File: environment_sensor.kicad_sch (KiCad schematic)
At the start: 121 parts, among them J1001 USB-C_USB4105-GF-A, J1002 SM04B-SRSS-TB-LF-SN, J1003 SM04B-SRSS-TB-LF-SN, U1001 FT4232H_VQFN, U1002 AP7370-33SA-7, U1003 STM32G474CET6, U1004 MB85RC1MTPNF-G, U1005 SHT45, U1006 BME280, Y1001 ABM3B-12.000MHZ-B2-T, Y1002 ECS-_327-12_5-34B-TR, Y1003 ABM3B-8.000MHZ-10-1-U-T

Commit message: Renumerate env sensor
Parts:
- renumbered BAT1001 to BAT1, C1038 to C104, C1039 to C105, C1040 to C106, C1001 to C56, C1002 to C57, C1003 to C59, C1004 to C60, C1005 to C62, C1006 to C63, C1007 to C64, C1008 to C65, C1009 to C67, C1010 to C68, C1011 to C69, C1012 to C70, C1013 to C71, C1014 to C72, C1015 to C73, C1016 to C74, C1017 to C75, C1018 to C76, C1019 to C77, C1020 to C78, C1021 to C79, C1022 to C80, C1023 to C81, C1024 to C82, C1025 to C83, C1026 to C84, C1027 to C85, C1028 to C86, C1029 to C87, C1030 to C88, C1031 to C89, C1032 to C90, C1033 to C91, C1034 to C92, C1035 to C93, C1036 to C94, C1037 to C95, D1001 to D36, D1002 to D37, D1003 to D38, D1004 to D39, D1005 to D40, D1006 to D41, D1007 to D42, D1008 to D43, D1009 to D44, FB1001 to FB13, FB1002 to FB14, FB1003 to FB15, FB1004 to FB16, FB1005 to FB17, J1001 to J17, J1002 to J18, J1003 to J20, LD1001 to LD1, LD1002 to LD2, MP1001 to MP10, MP1002 to MP11, MP1003 to MP12, R1001 to R250, R1002 to R251, R1003 to R252, R1004 to R253, R1005 to R254, R1006 to R255, R1007 to R256, R1008 to R257, R1009 to R258, R1010 to R259, R1011 to R260, R1012 to R261, R1013 to R262, R1014 to R263, R1015 to R264, R1016 to R265, R1017 to R266, R1018 to R267, R1019 to R268, R1020 to R269, R1021 to R270, R1022 to R271, R1023 to R272, R1024 to R273, R1025 to R274, R1026 to R275, R1027 to R276, R1028 to R277, R1029 to R278, R1030 to R279, R1031 to R280, R1032 to R281, R1033 to R282, R1034 to R283, R1035 to R284, R1036 to R285, R1037 to R286, R1038 to R287, R1039 to R288, R1040 to R289, TP1001 to TP6, TP1002 to TP60, TP1003 to TP61, TP1004 to TP62, TP1005 to TP63, TP1006 to TP64, TP1007 to TP65, TP1008 to TP66, TP1009 to TP67, U1001 to U11, U1002 to U27, U1003 to U28, U1004 to U29, U1005 to U30, U1006 to U31, Y1001 to Y2, Y1002 to Y3, Y1003 to Y4

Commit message: Change USB and mechanical points
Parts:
- removed J17: USB-C_USB4105-GF-A, antmicro-footprints:USB-C_GCT_USB4105-GF-A, symbol environment-sensor:USB-C_USB4105-GF-A
- removed MP10, MP11, MP12: PCB_Mount_Hole_2.7mm_M2.5_pad, antmicro-footprints:mounting-hole-2.7mm-M2.5-Pad, symbol environment-sensor:PCB_Mount_Hole_2.7mm_M2.5_pad
- added J17: USB-C_GCT_USB4145-03-0070-C, antmicro-footprints:USB-C_Receptacle_GCT_USB4145-03-0070-C, symbol antmicroUSBConnectors:USB-C_GCT_USB4145-03-0070-C
- added MP10, MP11, MP12: MP_Pad5.4mm_Drill2.7mm, antmicro-footprints:MP_Pad5.4mm_Drill2.7mm, symbol antmicroMechanicalParts:MP_Pad5.4mm_Drill2.7mm
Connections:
- net GND: now also J17.A1 (GND), J17.A12 (GND), J17.B1 (GND), J17.B12 (GND)
- net GNDREF: now also J17.SH
- net USB_CC1: now also J17.A5 (CC_{1})
- net USB_CC2: now also J17.B5 (CC_{2})
- net USB_D_N: now also J17.A7 (D_{A}-), J17.B7 (D_{B}-)
- net USB_D_P: now also J17.A6 (D_{A}+), J17.B6 (D_{B}+)
- net VBUS: now also J17.A4 (VBUS), J17.A9 (VBUS), J17.B4 (VBUS), J17.B9 (VBUS)
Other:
- moved on the sheet: BAT1, C104, C105, C106, C56, C57, C59, C60, C62, C63, C64, C65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

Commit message: Separate 3v3 labels on env sensor
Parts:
- added R? (x2): R_0R_0402, antmicro-footprints:R_0402_1005Metric, symbol antmicroResistors0402:R_0R_0402
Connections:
- net +3V3: now also R?.2; no longer C104.1, C105.2, C106.1, C56.2, C59.2, C62.2, C71.2, C72.2, C73.2, C79.2, C80.1, C81.2, C82.2, C84.2, C85.1, C87.2, C88.2, C95.1, D42.1, D44.1, FB13.1, FB14.1, FB17.2, J18.2, J20.2, R253.1, R272.2, R279.2, R280.2, R282.2, R284.2, R286.1, R288.2, R289.2, TP64.1, U11.16 (V_{CCIO}), U11.36 (V_{CCIO}), U11.44 (V_{REGIN}), U11.50 (V_{CCIO}), U27.2 (VOUT), U28.24 (VDD), U28.36 (VDD), U28.48 (VDD), U29.8 (VDD), U30.3 (VDD), U31.2 (CSB), U31.6 (VDDIO), U31.8 (VDD)
- new net: R?.2, U27.2 (VOUT)
- new net 3V3_ENV: C104.1, C105.2, C106.1, C56.2, C59.2, C62.2, C71.2, C72.2, C73.2, C79.2, C80.1, C81.2, C82.2, C84.2, C85.1, C87.2, C88.2, C95.1, D42.1, D44.1, FB13.1, FB14.1, FB17.2, J18.2, J20.2, R253.1, R272.2, R279.2, R280.2, R282.2, R284.2, R286.1, R288.2, R289.2, R?.1, R?.1, TP64.1, U11.16 (V_{CCIO}), U11.36 (V_{CCIO}), U11.44 (V_{REGIN}), U11.50 (V_{CCIO}), U28.24 (VDD), U28.36 (VDD), U28.48 (VDD), U29.8 (VDD), U30.3 (VDD), U31.2 (CSB), U31.6 (VDDIO), U31.8 (VDD)
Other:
- moved on the sheet: R279

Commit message: Fix tp on env sensor
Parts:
- removed TP6, TP60, TP61, TP62, TP63, TP64, TP65, TP66, TP67: TP_1mm_SMD, antmicro-footprints:Testpoint_smd_1mm, symbol environment-sensor:TP_1mm_SMD
- added TP6, TP60, TP61, TP62, TP63, TP64, TP65, TP66, TP67: TP_1mm_SMD, antmicro-footprints:TP_SMD_1mm, symbol antmicroTestPoints:TP_1mm_SMD
- gave numbers to parts that had none: 2
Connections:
- net 3V3_ENV: now also TP64.1
- net FRAM_WP: now also TP62.1
- net FTDI_+1V8: now also TP6.1
- net GND: now also TP65.1
- net I2C_1_SCL: now also TP67.1
- net I2C_1_SDA: now also TP66.1
- net at U11.30 (~{SUSPEND}): now also TP61.1
- net at R277.1, R280.1, R281.2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: now also TP63.1
- net at U11.54 (~{PWR_{EN}}): now also TP60.1

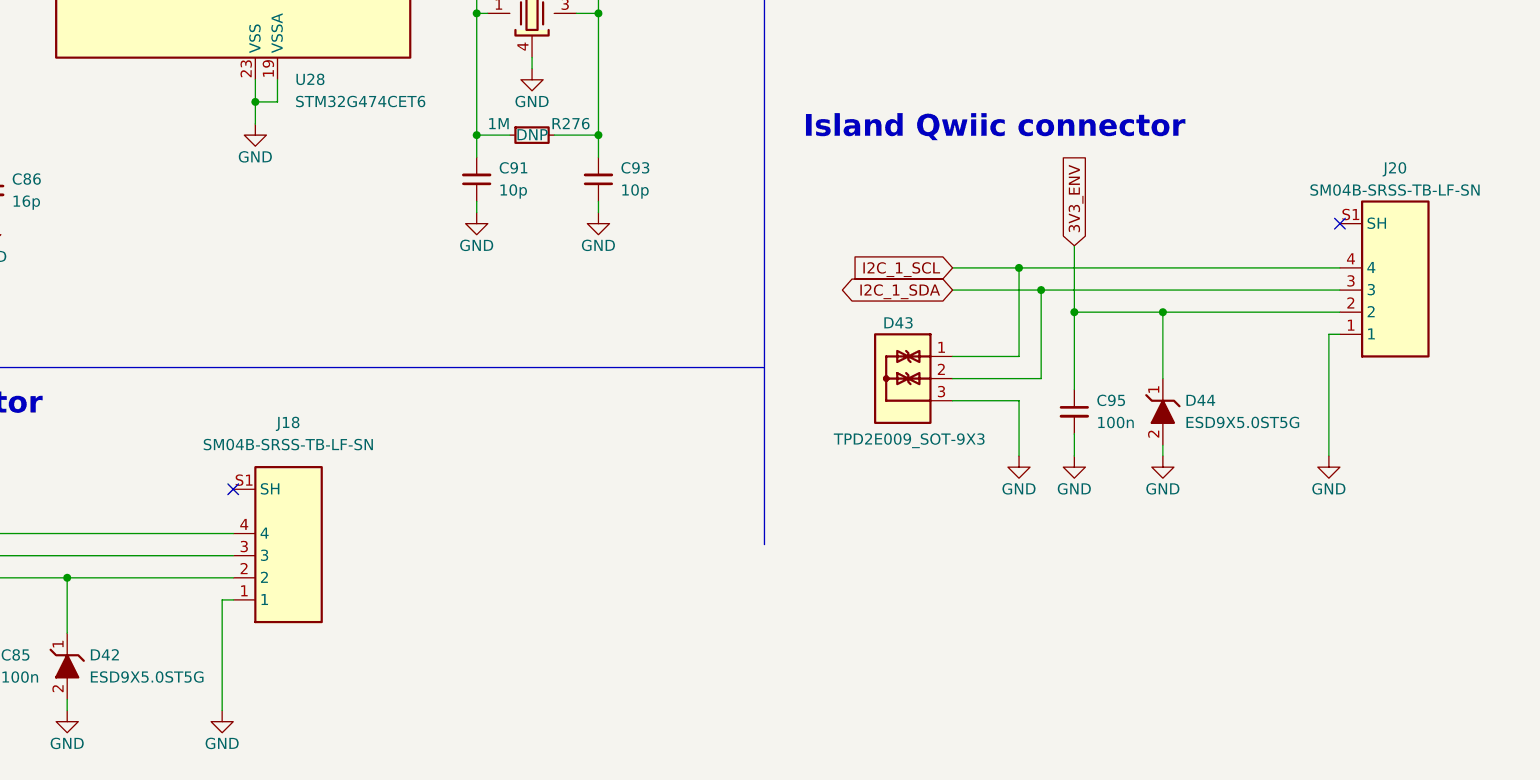
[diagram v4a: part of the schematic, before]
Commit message: Replace connectors on env sensor
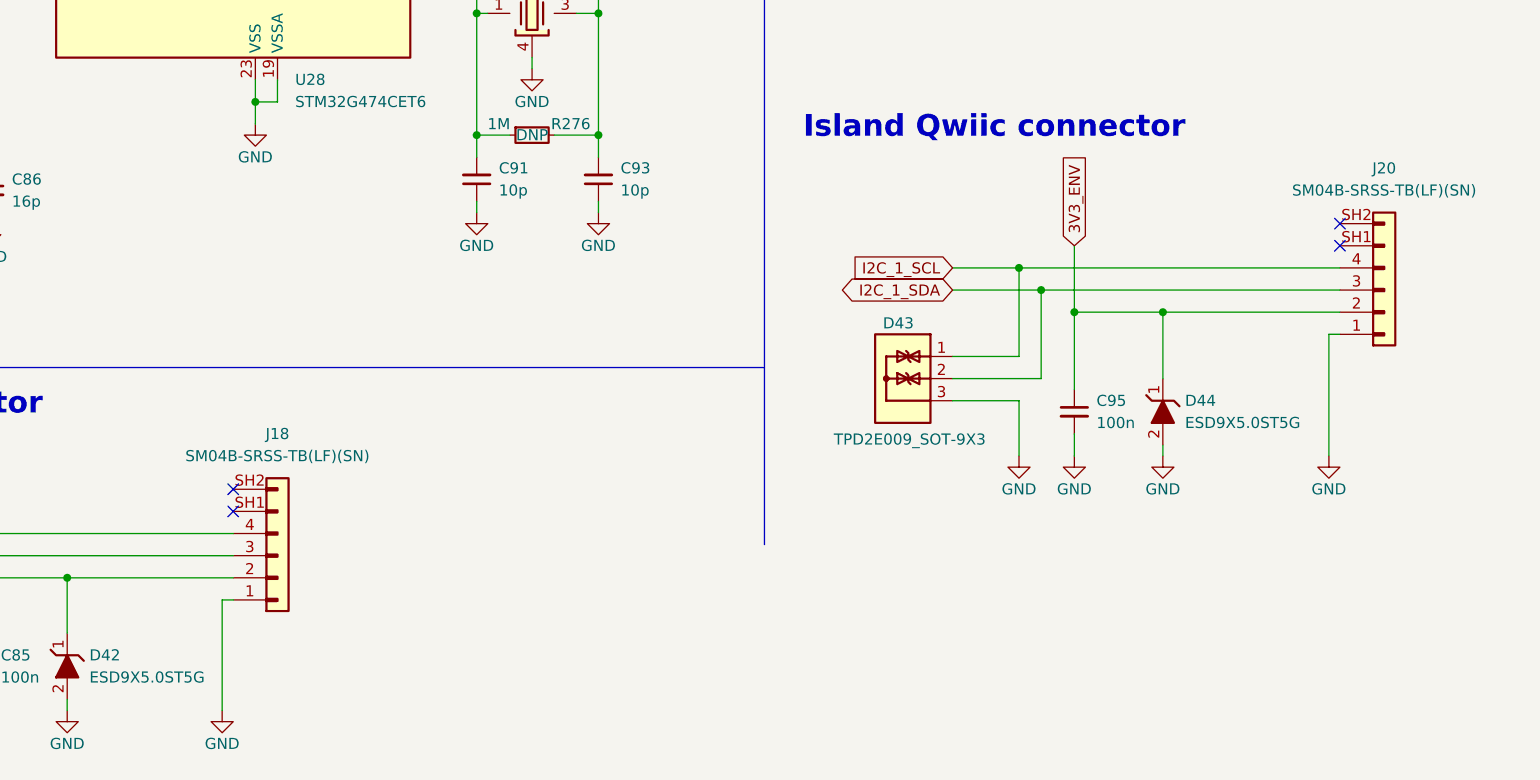
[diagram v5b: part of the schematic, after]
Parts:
- removed J18, J20: SM04B-SRSS-TB-LF-SN, antmicro-footprints:SM04B-SRSS-TB-LF-SN, symbol environment-sensor:SM04B-SRSS-TB-LF-SN
- added J18, J20: JST_SH_1x4_SM04B-SRSS-TB-LF-SN, antmicro-footprints:Conn_JST_SH_1x4_SM04B-SRSS-TB-LF-SN, symbol antmicroWire2BoardConnectors:JST_SH_1x4_SM04B-SRSS-TB-LF-SN
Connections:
- net 3V3_ENV: now also J18.2, J20.2
- net GND: now also J18.1, J20.1
- net I2C_1_SCL: now also J18.4, J20.4
- net I2C_1_SDA: now also J18.3, J20.3
- no-connect marks 48 -> 50
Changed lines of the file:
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@@
   (no_connect (at 281.94 140.97))
   (no_connect (at 281.94 179.07))
+  (no_connect (at 386.08 218.44))
   (no_connect (at 142.24 203.2))
   (no_connect (at 281.94 153.67))
@@
   (no_connect (at 130.81 276.86))
   (no_connect (at 281.94 173.99))
+  (no_connect (at 259.08 248.92))
   (no_connect (at 281.94 166.37))
   (no_connect (at 142.24 167.64))
@@
     (pin "2")
   )
+  (symbol (lib_id "antmicroWire2BoardConnectors:JST_SH_1x4_SM04B-SRSS-TB-LF-SN") (at 386.08 228.6 0) (mirror x) (unit 1)
+    (in_bom yes) (on_board yes) (fields_autoplaced)
+    (property "Reference" "J20" (id 0) (at 391.16 209.55 0)
+      (effects (font (size 1.27 1.27) (thickness 0.15)))
+    )
+    (property "Value" "JST_SH_1x4_SM04B-SRSS-TB-LF-SN" (id 1) (at 412.75 220.98 0)
+      (effects (font (size 1.27 1.27) (thickness 0.15)) (justify left bottom) hide)
+    )
+    (property "Footprint" "antmicro-footprints:Conn_JST_SH_1x4_SM04B-SRSS-TB-LF-SN" (id 2) (at 412.75 218.44 0)
+      (effects (font (size 1.27 1.27) (thickness 0.15)) (justify left bottom) hide)
+    )
+    (property "Datasheet" "https://www.jst-mfg.com/product/pdf/eng/eSH.pdf" (id 3) (at 412.75 215.9 0)
+      (effects (font (size 1.27 1.27) (thickness 0.15)) (justify left bottom) hide)
+    )
+    (property "MPN" "SM04B-SRSS-TB(LF)(SN)" (id 4) (at 391.16 212.09 0)
+      (effects (font (size 1.27 1.27) (thickness 0.15)))
+    )
+    (property "Manufacturer" "JST Automotive Connectors" (id 5) (at 412.75 213.36 0)
+      (effects (font (size 1.27 1.27) (thickness 0.15)) (justify left bottom) hide)
+    )
+    (property "Author" "Antmicro" (id 6) (at 412.75 210.82 0)
+      (effects (font (size 1.27 1.27) (thickness 0.15)) (justify left bottom) hide)
+    )
+    (property "License" "Apache-2.0" (id 7) (at 412.75 208.28 0)
+      (effects (font (size 1.27 1.27) (thickness 0.15)) (justify left bottom) hide)
+    )
+    (pin "1")
+    (pin "2")
+    (pin "3")
+    (pin "4")
+    (pin "SH1")
+    (pin "SH2")
+  )
   (symbol (lib_id "environment-sensor:R_100k_0402") (at 304.8 148.59 90) (unit 1)
     (in_bom yes) (on_board yes)
@@
     (pin "1")
   )
+  (symbol (lib_id "antmicroWire2BoardConnectors:JST_SH_1x4_SM04B-SRSS-TB-LF-SN") (at 259.08 259.08 0) (mirror x) (unit 1)
+    (in_bom yes) (on_board yes) (fields_autoplaced)
+    (property "Reference" "J18" (id 0) (at 264.16 240.03 0)
+      (effects (font (size 1.27 1.27) (thickness 0.15)))
+    )
+    (property "Value" "JST_SH_1x4_SM04B-SRSS-TB-LF-SN" (id 1) (at 285.75 251.46 0)
+      (effects (font (size 1.27 1.27) (thickness 0.15)) (justify left bottom) hide)
+    )
+    (property "Footprint" "antmicro-footprints:Conn_JST_SH_1x4_SM04B-SRSS-TB-LF-SN" (id 2) (at 285.75 248.92 0)
+      (effects (font (size 1.27 1.27) (thickness 0.15)) (justify left bottom) hide)
+    )
+    (property "Datasheet" "https://www.jst-mfg.com/product/pdf/eng/eSH.pdf" (id 3) (at 285.75 246.38 0)
+      (effects (font (size 1.27 1.27) (thickness 0.15)) (justify left bottom) hide)
+    )
+    (property "MPN" "SM04B-SRSS-TB(LF)(SN)" (id 4) (at 264.16 242.57 0)
+      (effects (font (size 1.27 1.27) (thickness 0.15)))
+    )
+    (property "Manufacturer" "JST Automotive Connectors" (id 5) (at 285.75 243.84 0)
+      (effects (font (size 1.27 1.27) (thickness 0.15)) (justify left bottom) hide)
+    )
+    (property "Author" "Antmicro" (id 6) (at 285.75 241.3 0)
+      (effects (font (size 1.27 1.27) (thickness 0.15)) (justify left bottom) hide)
+    )
+    (property "License" "Apache-2.0" (id 7) (at 285.75 238.76 0)
+      (effects (font (size 1.27 1.27) (thickness 0.15)) (justify left bottom) hide)
+    )
+    (pin "1")
+    (pin "2")
+    (pin "3")
+    (pin "4")
+    (pin "SH1")
+    (pin "SH2")
+  )
   (symbol (lib_id "environment-sensor:GND") (at 240.03 271.78 0) (mirror y) (unit 1)
     (in_bom yes) (on_board yes)
@@
     (pin "1")
   )
-  (symbol (lib_id "environment-sensor:SM04B-SRSS-TB-LF-SN") (at 386.08 228.6 0) (mirror x) (unit 1)
-    (in_bom yes) (on_board yes)
-    (property "Reference" "J20" (id 0) (at 392.43 209.55 0)
-      (effects (font (size 1.27 1.27) (thickness 0.15)))
-    )
-    (property "Value" "SM04B-SRSS-TB-LF-SN" (id 1) (at 392.43 212.09 0)
-      (effects (font (size 1.27 1.27) (thickness 0.15)))
-    )
-    (property "Footprint" "antmicro-footprints:SM04B-SRSS-TB-LF-SN" (id 2) (at 412.75 219.71 0)
-      (effects (font (size 1.27 1.27) (thickness 0.15)) (justify left bottom) hide)
-    )
-    (property "Datasheet" "https://www.jst-mfg.com/product/pdf/eng/eSH.pdf" (id 3) (at 412.75 217.17 0)
-      (effects (font (size 1.27 1.27) (thickness 0.15)) (justify left bottom) hide)
-    )
-    (property "MPN" "SM04B-SRSS-TB(LF)(SN)" (id 4) (at 412.75 214.63 0)
-      (effects (font (size 1.27 1.27) (thickness 0.15)) (justify left bottom) hide)
-    )
-    (property "Manufacturer" "JST" (id 5) (at 412.75 212.09 0)
-      (effects (font (size 1.27 1.27) (thickness 0.15)) (justify left bottom) hide)
-    )
-    (property "Author" "Antmicro" (id 6) (at 412.75 209.55 0)
-      (effects (font (size 1.27 1.27) (thickness 0.15)) (justify left bottom) hide)
-    )
-    (property "License" "Apache-2.0" (id 7) (at 412.75 207.01 0)
-      (effects (font (size 1.27 1.27) (thickness 0.15)) (justify left bottom) hide)
-    )
-    (pin "1")
-    (pin "2")
-    (pin "3")
-    (pin "4")
-    (pin "S1")
-    (pin "S2")
-  )
   (symbol (lib_id "environment-sensor:PWR_FLAG") (at 167.64 46.99 0) (unit 1)
     (in_bom yes) (on_board yes)
@@
     (pin "1")
   )
-  (symbol (lib_id "environment-sensor:SM04B-SRSS-TB-LF-SN") (at 259.08 259.08 0) (mirror x) (unit 1)
-    (in_bom yes) (on_board yes) (fields_autoplaced)
-    (property "Reference" "J18" (id 0) (at 265.43 238.76 0)
-      (effects (font (size 1.27 1.27) (thickness 0.15)))
-    )
-    (property "Value" "SM04B-SRSS-TB-LF-SN" (id 1) (at 265.43 241.3 0)
-      (effects (font (size 1.27 1.27) (thickness 0.15)))
-    )
-    (property "Footprint" "antmicro-footprints:SM04B-SRSS-TB-LF-SN" (id 2) (at 285.75 250.19 0)
-      (effects (font (size 1.27 1.27) (thickness 0.15)) (justify left bottom) hide)
-    )
-    (property "Datasheet" "https://www.jst-mfg.com/product/pdf/eng/eSH.pdf" (id 3) (at 285.75 247.65 0)
-      (effects (font (size 1.27 1.27) (thickness 0.15)) (justify left bottom) hide)
-    )
-    (property "MPN" "SM04B-SRSS-TB(LF)(SN)" (id 4) (at 285.75 245.11 0)
-      (effects (font (size 1.27 1.27) (thickness 0.15)) (justify left bottom) hide)
-    )
-    (property "Manufacturer" "JST" (id 5) (at 285.75 242.57 0)
-      (effects (font (size 1.27 1.27) (thickness 0.15)) (justify left bottom) hide)
-    )
-    (property "Author" "Antmicro" (id 6) (at 285.75 240.03 0)
-      (effects (font (size 1.27 1.27) (thickness 0.15)) (justify left bottom) hide)
-    )
-    (property "License" "Apache-2.0" (id 7) (at 285.75 237.49 0)
-      (effects (font (size 1.27 1.27) (thickness 0.15)) (justify left bottom) hide)
-    )
-    (pin "1")
-    (pin "2")
-    (pin "3")
-    (pin "4")
-    (pin "S1")
-    (pin "S2")
-  )
   (symbol (lib_id "environment-sensor:FB_120Z_2A_0603") (at 29.21 181.61 0) (unit 1)

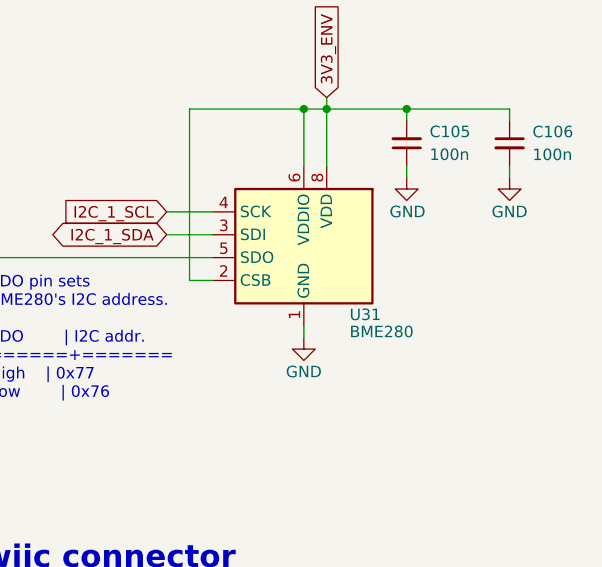
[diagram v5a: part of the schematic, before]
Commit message: Fix BME280
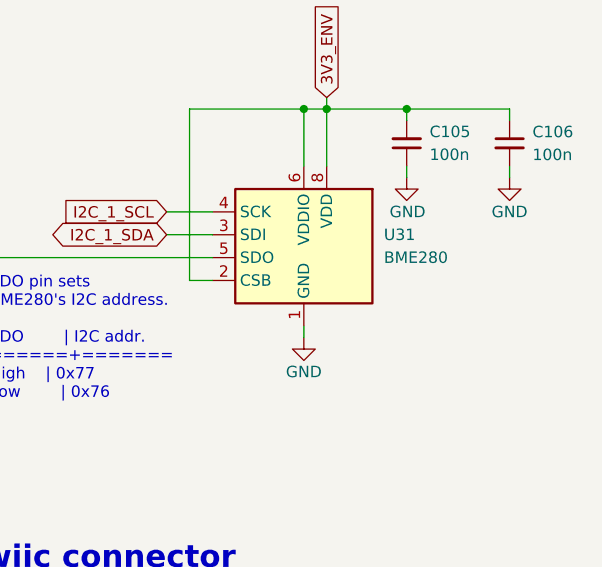
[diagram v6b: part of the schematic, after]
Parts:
- removed U31: BME280, antmicro-footprints:Pressure_Sensor_LGA-8_2.5x2.5mm_BME280, symbol environment-sensor:BME280
- added U31: BME280, antmicro-footprints:LGA-8_2.5x2.5mm_BME280, symbol antmicroHumidityMoistureSensors:BME280
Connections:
- net 3V3_ENV: now also U31.2 (CSB), U31.6 (VDDIO), U31.8 (VDD)
- net GND: now also U31.1 (GND), U31.7 (GND)
- net I2C_1_SCL: now also U31.4 (SCK)
- net I2C_1_SDA: now also U31.3 (SDI)
- net at R286.2, R287.2: now also U31.5 (SDO)
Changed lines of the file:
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@@
     (pin "2")
-  )
-  (symbol (lib_id "environment-sensor:BME280") (at 365.76 161.29 0) (unit 1)
-    (in_bom yes) (on_board yes)
-    (property "Reference" "U31" (id 0) (at 381 177.8 0)
-      (effects (font (size 1.27 1.27)) (justify left))
-    )
-    (property "Value" "BME280" (id 1) (at 381 179.705 0)
-      (effects (font (size 1.27 1.27) (thickness 0.15)) (justify left))
-    )
-    (property "Footprint" "antmicro-footprints:Pressure_Sensor_LGA-8_2.5x2.5mm_BME280" (id 2) (at 398.78 171.45 0)
-      (effects (font (size 1.27 1.27) (thickness 0.15)) (justify left bottom) hide)
-    )
-    (property "Datasheet" "https://www.bosch-sensortec.com/media/boschsensortec/downloads/datasheets/bst-bme280-ds002.pdf" (id 3) (at 398.78 173.99 0)
-      (effects (font (size 1.27 1.27) (thickness 0.15)) (justify left bottom) hide)
-    )
-    (property "MPN" "BME280" (id 4) (at 398.78 176.53 0)
-      (effects (font (size 1.27 1.27) (thickness 0.15)) (justify left bottom) hide)
-    )
-    (property "Manufacturer" "Bosch Sensortec" (id 5) (at 398.78 179.07 0)
-      (effects (font (size 1.27 1.27) (thickness 0.15)) (justify left bottom) hide)
-    )
-    (property "Author" "Antmicro" (id 6) (at 398.78 181.61 0)
-      (effects (font (size 1.27 1.27) (thickness 0.15)) (justify left bottom) hide)
-    )
-    (property "License" "Apache-2.0" (id 7) (at 398.78 184.15 0)
-      (effects (font (size 1.27 1.27) (thickness 0.15)) (justify left bottom) hide)
-    )
-    (pin "1")
-    (pin "2")
-    (pin "3")
-    (pin "4")
-    (pin "5")
-    (pin "6")
-    (pin "7")
-    (pin "8")
   )
   (symbol (lib_id "environment-sensor:C_100n_0402") (at 40.64 224.79 90) (mirror x) (unit 1)
@@
     (pin "2")
   )
+  (symbol (lib_id "antmicroHumidityMoistureSensors:BME280") (at 365.76 161.29 0) (unit 1)
+    (in_bom yes) (on_board yes) (fields_autoplaced)
+    (property "Reference" "U31" (id 0) (at 384.81 168.9099 0)
+      (effects (font (size 1.27 1.27) (thickness 0.15)) (justify left))
+    )
+    (property "Value" "BME280" (id 1) (at 384.81 171.4499 0)
+      (effects (font (size 1.27 1.27) (thickness 0.15)) (justify left))
+    )
+    (property "Footprint" "antmicro-footprints:LGA-8_2.5x2.5mm_BME280" (id 2) (at 398.78 171.45 0)
+      (effects (font (size 1.27 1.27) (thickness 0.15)) (justify left bottom) hide)
+    )
+    (property "Datasheet" "https://www.bosch-sensortec.com/media/boschsensortec/downloads/datasheets/bst-bme280-ds002.pdf" (id 3) (at 398.78 173.99 0)
+      (effects (font (size 1.27 1.27) (thickness 0.15)) (justify left bottom) hide)
+    )
+    (property "MPN" "BME280" (id 4) (at 398.78 176.53 0)
+      (effects (font (size 1.27 1.27) (thickness 0.15)) (justify left bottom) hide)
+    )
+    (property "Manufacturer" "Bosch" (id 5) (at 398.78 179.07 0)
+      (effects (font (size 1.27 1.27) (thickness 0.15)) (justify left bottom) hide)
+    )
+    (property "Author" "Antmicro" (id 6) (at 398.78 181.61 0)
+      (effects (font (size 1.27 1.27) (thickness 0.15)) (justify left bottom) hide)
+    )
+    (property "License" "Apache-2.0" (id 7) (at 398.78 184.15 0)
+      (effects (font (size 1.27 1.27) (thickness 0.15)) (justify left bottom) hide)
+    )
+    (pin "1")
+    (pin "2")
+    (pin "3")
+    (pin "4")
+    (pin "5")
+    (pin "6")
+    (pin "7")
+    (pin "8")
+  )
   (symbol (lib_id "environment-sensor:R_12k_0402") (at 95.25 238.76 90) (unit 1)
